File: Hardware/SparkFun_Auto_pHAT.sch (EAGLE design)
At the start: 146 parts, among them J11 EXT MTR PWR, J18 ISP, J2 RASPBERRYPI-40-PIN-GPIO_SMD_S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, J20 USB C, J23 CORTEX_JTAG_DEBUG_PTH, J7 EXT SERVO PWR, J8 EXT 5V PWR, Q1 310mA/60V/1.6Ω, Q23 20V/0.2A/8MHz/1.2Ω/1Vth, Q24 20V/0.2A/8MHz/1.2Ω/1Vth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

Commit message: v12
-moved stat LED to side for easier rework and better visibility
-added holes to let air through to SHIM Fan (when it sits flush up to the PCB, there is no room for airflow)
-bumped version to v12 in copper and all 3 sheets in sch
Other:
- note added: "v12"
- note removed: "v11"
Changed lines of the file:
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@@
 <plain>
 <text x="349.758" y="11.43" size="2.54" layer="94" font="vector">Pete Lewis</text>
-<text x="421.64" y="6.604" size="2.54" layer="94" font="vector" ratio="12">v11</text>
+<text x="421.64" y="6.604" size="2.54" layer="94" font="vector" ratio="12">v12</text>
 <wire x1="139.7" y1="152.4" x2="139.7" y2="91.44" width="0.3048" layer="97" style="longdash"/>
 <wire x1="139.7" y1="91.44" x2="139.7" y2="0" width="0.3048" layer="97" style="longdash"/>
@@
 <text x="166.624" y="11.43" size="2.54" layer="94" font="vector">Pete Lewis</text>
 <text x="5.08" y="177.8" size="3.81" layer="94" font="vector">Motor Driver IC - PSoC I/O</text>
-<text x="237.49" y="7.62" size="2.54" layer="94" font="vector">v11</text>
+<text x="237.49" y="7.62" size="2.54" layer="94" font="vector">v12</text>
 <text x="123.698" y="18.288" size="1.27" layer="97" font="vector" rot="MR180">P3.2 swd_io[0]
 P3.3 swd_clk[0]
@@
 <text x="261.874" y="11.176" size="1.778" layer="97" font="vector">*For frame synchronization support
 (3.3V Logic level)</text>
-<text x="421.386" y="7.366" size="2.54" layer="94" font="vector">v11</text>
+<text x="421.386" y="7.366" size="2.54" layer="94" font="vector">v12</text>
 <text x="349.758" y="11.43" size="2.54" layer="94" font="vector">Pete Lewis</text>
 </plain>

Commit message: Adjusted screwpin terminal fp and locations to work with 1x2s and 1x6s
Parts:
- J13, J14, J16, J9: device SparkFun-Connectors:CONN_022.54MM_SCREWTERM -> autophat:CONN_02LG_DRILL
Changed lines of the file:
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@@
 <grid distance="0.1" unitdist="inch" unit="inch" style="lines" multiple="1" display="no" altdistance="0.01" altunitdist="inch" altunit="inch"/>
 <layers>
-<layer number="1" name="Top" color="4" fill="1" visible="no" active="no"/>
-<layer number="2" name="Route2" color="1" fill="3" visible="no" active="no"/>
-<layer number="3" name="Route3" color="4" fill="3" visible="no" active="no"/>
-<layer number="4" name="Route4" color="1" fill="4" visible="no" active="no"/>
-<layer number="5" name="Route5" color="4" fill="4" visible="no" active="no"/>
-<layer number="6" name="Route6" color="1" fill="8" visible="no" active="no"/>
-<layer number="7" name="Route7" color="4" fill="8" visible="no" active="no"/>
-<layer number="8" name="Route8" color="1" fill="2" visible="no" active="no"/>
-<layer number="9" name="Route9" color="4" fill="2" visible="no" active="no"/>
-<layer number="10" name="Route10" color="1" fill="7" visible="no" active="no"/>
-<layer number="11" name="Route11" color="4" fill="7" visible="no" active="no"/>
-<layer number="12" name="Route12" color="1" fill="5" visible="no" active="no"/>
-<layer number="13" name="Route13" color="4" fill="5" visible="no" active="no"/>
-<layer number="14" name="Route14" color="1" fill="6" visible="no" active="no"/>
-<layer number="15" name="Route15" color="4" fill="6" visible="no" active="no"/>
-<layer number="16" name="Bottom" color="1" fill="1" visible="no" active="no"/>
-<layer number="17" name="Pads" color="2" fill="1" visible="no" active="no"/>
-<layer number="18" name="Vias" color="2" fill="1" visible="no" active="no"/>
-<layer number="19" name="Unrouted" color="6" fill="1" visible="no" active="no"/>
-<layer number="20" name="Dimension" color="24" fill="1" visible="no" active="no"/>
-<layer number="21" name="tPlace" color="16" fill="1" visible="no" active="no"/>
-<layer number="22" name="bPlace" color="14" fill="1" visible="no" active="no"/>
-<layer number="23" name="tOrigins" color="15" fill="1" visible="no" active="no"/>
-<layer number="24" name="bOrigins" color="15" fill="1" visible="no" active="no"/>
-<layer number="25" name="tNames" color="7" fill="1" visible="no" active="no"/>
-<layer number="26" name="bNames" color="7" fill="1" visible="no" active="no"/>
-<layer number="27" name="tValues" color="7" fill="1" visible="no" active="no"/>
-<layer number="28" name="bValues" color="7" fill="1" visible="no" active="no"/>
+<layer number="1" name="Top" color="4" fill="1" visible="yes" active="no"/>
+<layer number="2" name="Route2" color="1" fill="3" visible="yes" active="no"/>
+<layer number="3" name="Route3" color="4" fill="3" visible="yes" active="no"/>
+<layer number="4" name="Route4" color="1" fill="4" visible="yes" active="no"/>
+<layer number="5" name="Route5" color="4" fill="4" visible="yes" active="no"/>
+<layer number="6" name="Route6" color="1" fill="8" visible="yes" active="no"/>
+<layer number="7" name="Route7" color="4" fill="8" visible="yes" active="no"/>
+<layer number="8" name="Route8" color="1" fill="2" visible="yes" active="no"/>
+<layer number="9" name="Route9" color="4" fill="2" visible="yes" active="no"/>
+<layer number="10" name="Route10" color="1" fill="7" visible="yes" active="no"/>
+<layer number="11" name="Route11" color="4" fill="7" visible="yes" active="no"/>
+<layer number="12" name="Route12" color="1" fill="5" visible="yes" active="no"/>
+<layer number="13" name="Route13" color="4" fill="5" visible="yes" active="no"/>
+<layer number="14" name="Route14" color="1" fill="6" visible="yes" active="no"/>
+<layer number="15" name="Route15" color="4" fill="6" visible="yes" active="no"/>
+<layer number="16" name="Bottom" color="1" fill="1" visible="yes" active="no"/>
+<layer number="17" name="Pads" color="2" fill="1" visible="yes" active="no"/>
+<layer number="18" name="Vias" color="2" fill="1" visible="yes" active="no"/>
+<layer number="19" name="Unrouted" color="6" fill="1" visible="yes" active="no"/>
+<layer number="20" name="Dimension" color="24" fill="1" visible="yes" active="no"/>
+<layer number="21" name="tPlace" color="16" fill="1" visible="yes" active="no"/>
+<layer number="22" name="bPlace" color="14" fill="1" visible="yes" active="no"/>
+<layer number="23" name="tOrigins" color="15" fill="1" visible="yes" active="no"/>
+<layer number="24" name="bOrigins" color="15" fill="1" visible="yes" active="no"/>
+<layer number="25" name="tNames" color="7" fill="1" visible="yes" active="no"/>
+<layer number="26" name="bNames" color="7" fill="1" visible="yes" active="no"/>
+<layer number="27" name="tValues" color="7" fill="1" visible="yes" active="no"/>
+<layer number="28" name="bValues" color="7" fill="1" visible="yes" active="no"/>
 <layer number="29" name="tStop" color="7" fill="3" visible="no" active="no"/>
 <layer number="30" name="bStop" color="7" fill="6" visible="no" active="no"/>
@@
 <layer number="35" name="tGlue" color="7" fill="4" visible="no" active="no"/>
 <layer number="36" name="bGlue" color="7" fill="5" visible="no" active="no"/>
-<layer number="37" name="tTest" color="7" fill="1" visible="no" active="no"/>
-<layer number="38" name="bTest" color="7" fill="1" visible="no" active="no"/>
+<layer number="37" name="tTest" color="7" fill="1" visible="yes" active="no"/>
+<layer number="38" name="bTest" color="7" fill="1" visible="yes" active="no"/>
 <layer number="39" name="tKeepout" color="4" fill="11" visible="no" active="no"/>
 <layer number="40" name="bKeepout" color="1" fill="11" visible="no" active="no"/>
@@
 <layer number="44" name="Drills" color="7" fill="1" visible="no" active="no"/>
 <layer number="45" name="Holes" color="7" fill="1" visible="no" active="no"/>
-<layer number="46" name="Milling" color="3" fill="1" visible="no" active="no"/>
-<layer number="47" name="Measures" color="7" fill="1" visible="no" active="no"/>
-<layer number="48" name="Document" color="13" fill="7" visible="no" active="no"/>
-<layer number="49" name="Reference" color="13" fill="1" visible="no" active="no"/>
-<layer number="50" name="dxf" color="7" fill="1" visible="no" active="no"/>
-<layer number="51" name="tDocu" color="6" fill="1" visible="no" active="no"/>
-<layer number="52" name="bDocu" color="7" fill="1" visible="no" active="no"/>
-<layer number="53" name="tGND_GNDA" color="7" fill="9" visible="no" active="no"/>
-<layer number="54" name="bGND_GNDA" color="1" fill="9" visible="no" active="no"/>
-<layer number="56" name="wert" color="7" fill="1" visible="no" active="no"/>
-<layer number="57" name="tCAD" color="7" fill="1" visible="no" active="no"/>
-<layer number="59" name="tCarbon" color="7" fill="1" visible="no" active="no"/>
-<layer number="60" name="bCarbon" color="7" fill="1" visible="no" active="no"/>
+<layer number="46" name="Milling" color="3" fill="1" visible="yes" active="no"/>
+<layer number="47" name="Measures" color="7" fill="1" visible="yes" active="no"/>
+<layer number="48" name="Document" color="13" fill="7" visible="yes" active="no"/>
+<layer number="49" name="Reference" color="13" fill="1" visible="yes" active="no"/>
+<layer number="50" name="dxf" color="7" fill="1" visible="yes" active="no"/>
+<layer number="51" name="tDocu" color="6" fill="1" visible="yes" active="no"/>
+<layer number="52" name="bDocu" color="7" fill="1" visible="yes" active="no"/>
+<layer number="53" name="tGND_GNDA" color="7" fill="9" visible="yes" active="no"/>
+<layer number="54" name="bGND_GNDA" color="1" fill="9" visible="yes" active="no"/>
+<layer number="56" name="wert" color="7" fill="1" visible="yes" active="no"/>
+<layer number="57" name="tCAD" color="7" fill="1" visible="yes" active="no"/>
+<layer number="59" name="tCarbon" color="7" fill="1" visible="yes" active="no"/>
+<layer number="60" name="bCarbon" color="7" fill="1" visible="yes" active="no"/>
 <layer number="88" name="SimResults" color="9" fill="1" visible="no" active="yes"/>
 <layer number="89" name="SimProbes" color="9" fill="1" visible="no" active="yes"/>
@@
 <part name="GND4" library="SparkFun-Aesthetics" deviceset="GND" device=""/>
 <part name="SUPPLY2" library="SparkFun-PowerSymbols" deviceset="3.3V" device=""/>
-<part name="J9" library="SparkFun-Connectors" deviceset="CONN_02" device="2.54MM_SCREWTERM"/>
+<part name="J9" library="autophat" deviceset="CONN_02" device="LG_DRILL"/>
 <part name="J12" library="SparkFun-Connectors" deviceset="CONN_02" device="2.54MM_SCREWTERM"/>
-<part name="J13" library="SparkFun-Connectors" deviceset="CONN_02" device="2.54MM_SCREWTERM"/>
-<part name="J14" library="SparkFun-Connectors" deviceset="CONN_02" device="2.54MM_SCREWTERM"/>
+<part name="J13" library="autophat" deviceset="CONN_02" device="LG_DRILL"/>
+<part name="J14" library="autophat" deviceset="CONN_02" device="LG_DRILL"/>
 <part name="J15" library="SparkFun-Connectors" deviceset="CONN_02" device="2.54MM_SCREWTERM"/>
-<part name="J16" library="SparkFun-Connectors" deviceset="CONN_02" device="2.54MM_SCREWTERM"/>
+<part name="J16" library="autophat" deviceset="CONN_02" device="LG_DRILL"/>
 <part name="J6" library="SparkFun-Connectors" deviceset="CONN_01" device="PTH_NO_SILK_YES_STOP"/>
 <part name="SUPPLY16" library="SparkFun-PowerSymbols" deviceset="3.3V" device=""/>

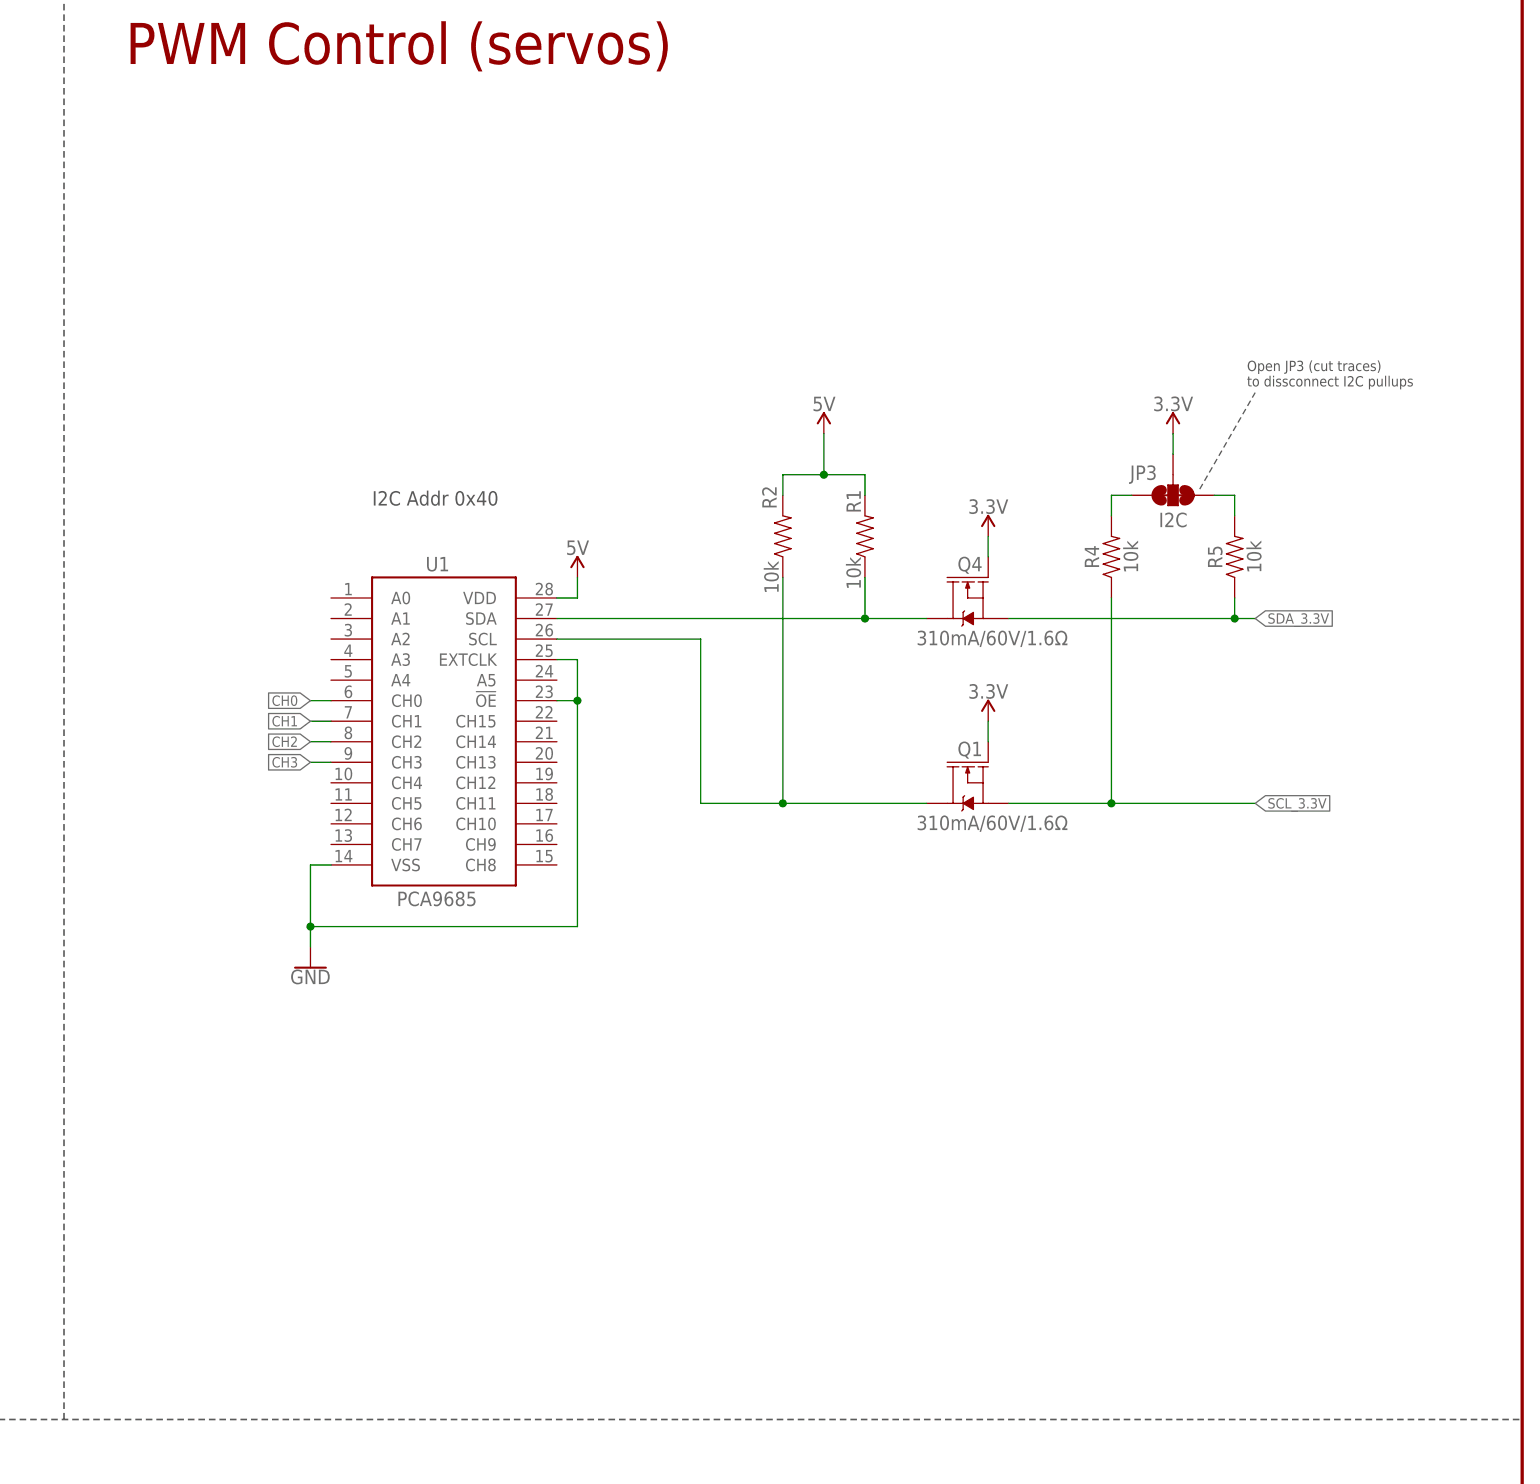
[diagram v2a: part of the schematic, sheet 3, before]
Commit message: Added Address jumpers for Servo IC
-Added 3 address jumpers to Servo IC. (includes a BOM change to include 3 more 10K resistors) This will allow for up to 8 different addresses. Note, A4 and A5 are permenantly connected to GND.
-Added address table to SCH for address jumpers.
-increased one of the "fan" holes to allow for even more airflow using the SHIM fan.
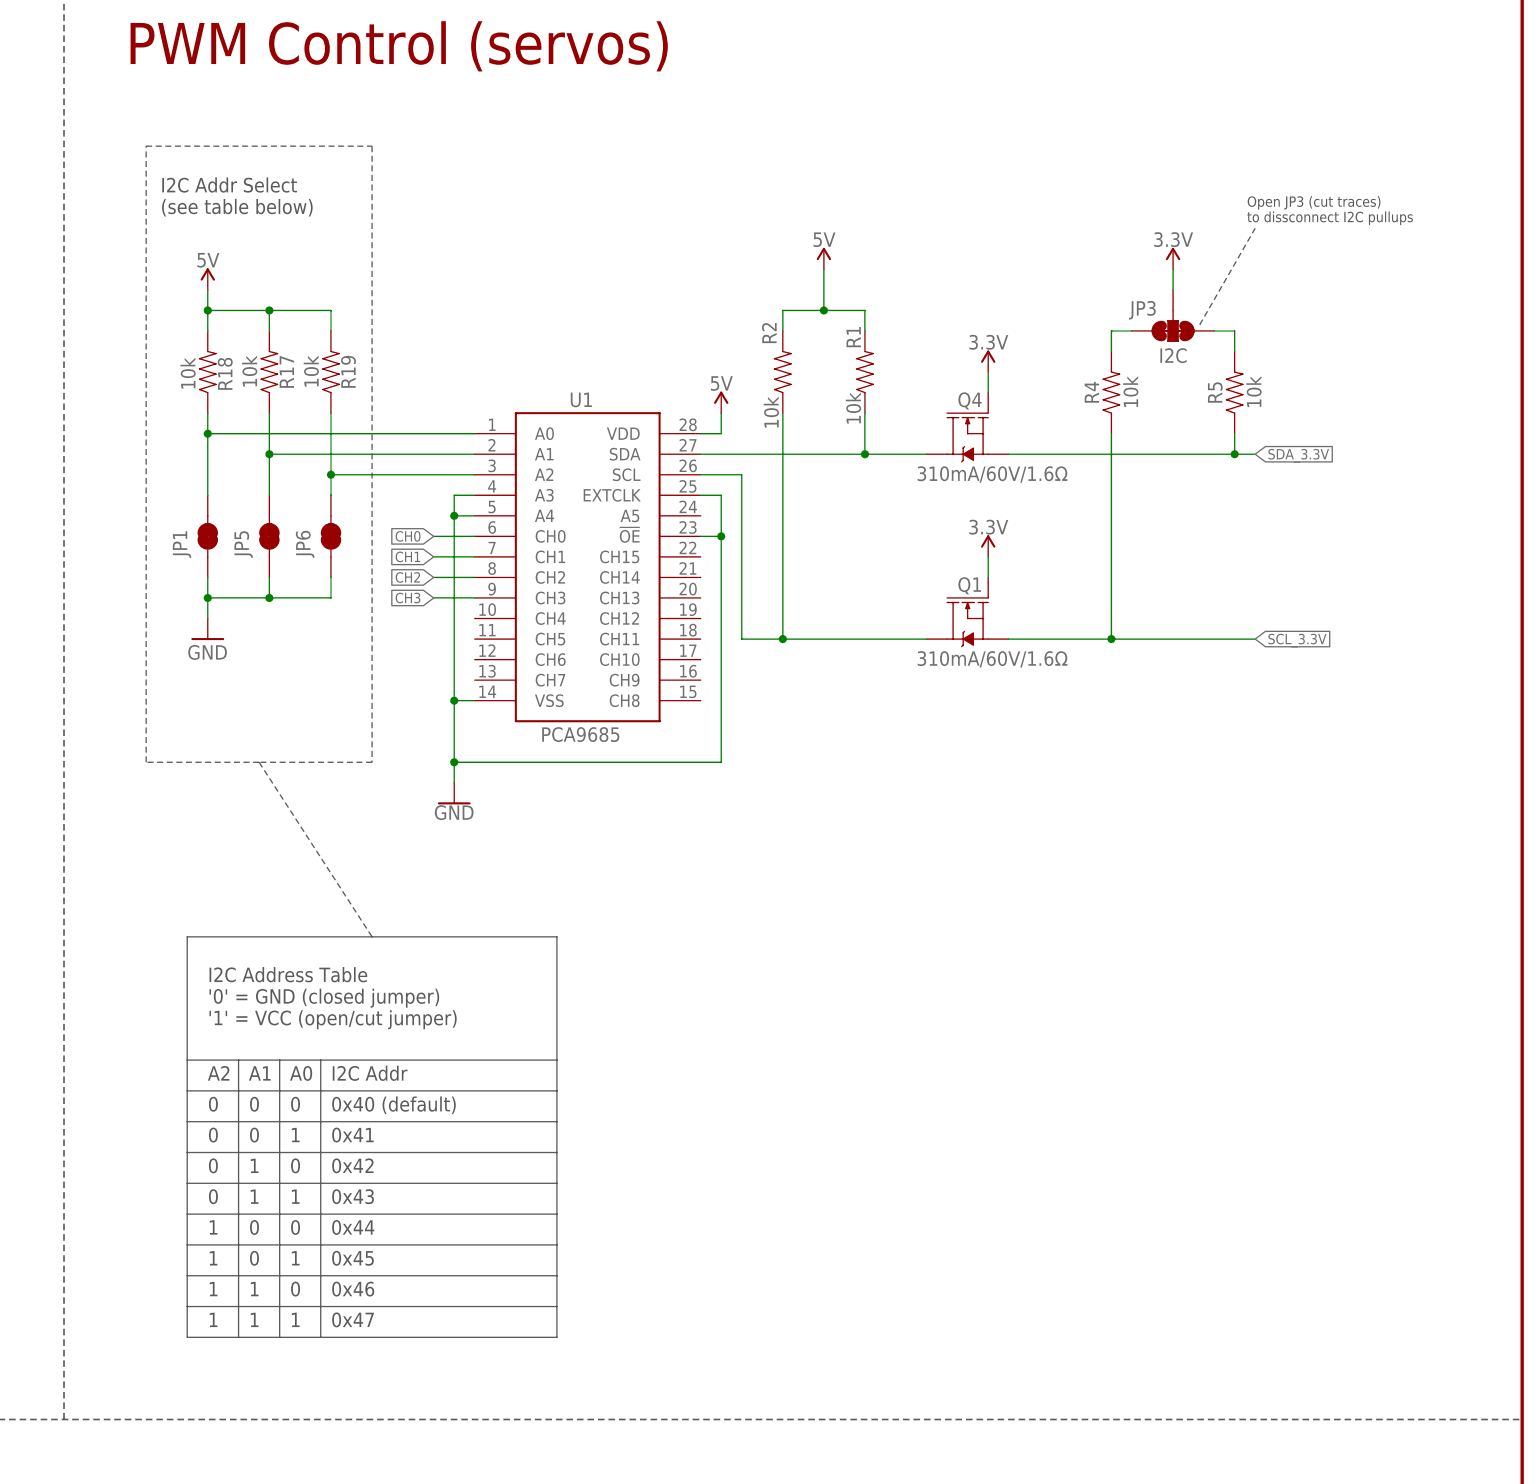
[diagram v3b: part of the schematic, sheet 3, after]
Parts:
- added JP1, JP5, JP6: JUMPER-PAD-2, SparkFun-Jumpers:JUMPER-SMT_2_NC_TRACE_NO-SILK
- added R17, R18, R19: 10k, SparkFun-Resistors:10KOHM-0603-1/10W-1%
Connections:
- new net ADD_A0: JP1.2, R18.1, U1.A0
- new net ADD_A1: JP5.2, R17.1, U1.A1
- new net ADD_A2: JP6.2, R19.1, U1.A2
- net 5V: now also R17.2, R18.2, R19.2
- net GND: now also JP1.1, JP5.1, JP6.1, U1.A3, U1.A4
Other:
- note added: "0"
- note added: "0x40 (default)"
- note added: "0x41"
- note added: "0x42"
- note added: "0x43"
- note added: "0x44"
- note added: "0x45"
- note added: "0x46"
- note added: "0x47"
- note added: "1"
- note added: "A0"
- note added: "A1"
- note added: "A2"
- note added: "I2C Addr"
- note added: "I2C Addr Select (see table below)"
- note added: "I2C Address Table '0' = GND (closed jumper) '1' = VCC (open/cut jumper)"
- note removed: "I2C Addr 0x40"
- moved on the sheet: JP3, Q1, Q4, R1, R2, R4, R5, U1
